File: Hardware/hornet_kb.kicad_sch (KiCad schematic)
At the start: 12 parts, among them J1 Conn_ST_STDC14, J10 USB_C_Receptacle_USB2.0, U1 nRF52840, Y1 32.768kHz, Y2 32MHz

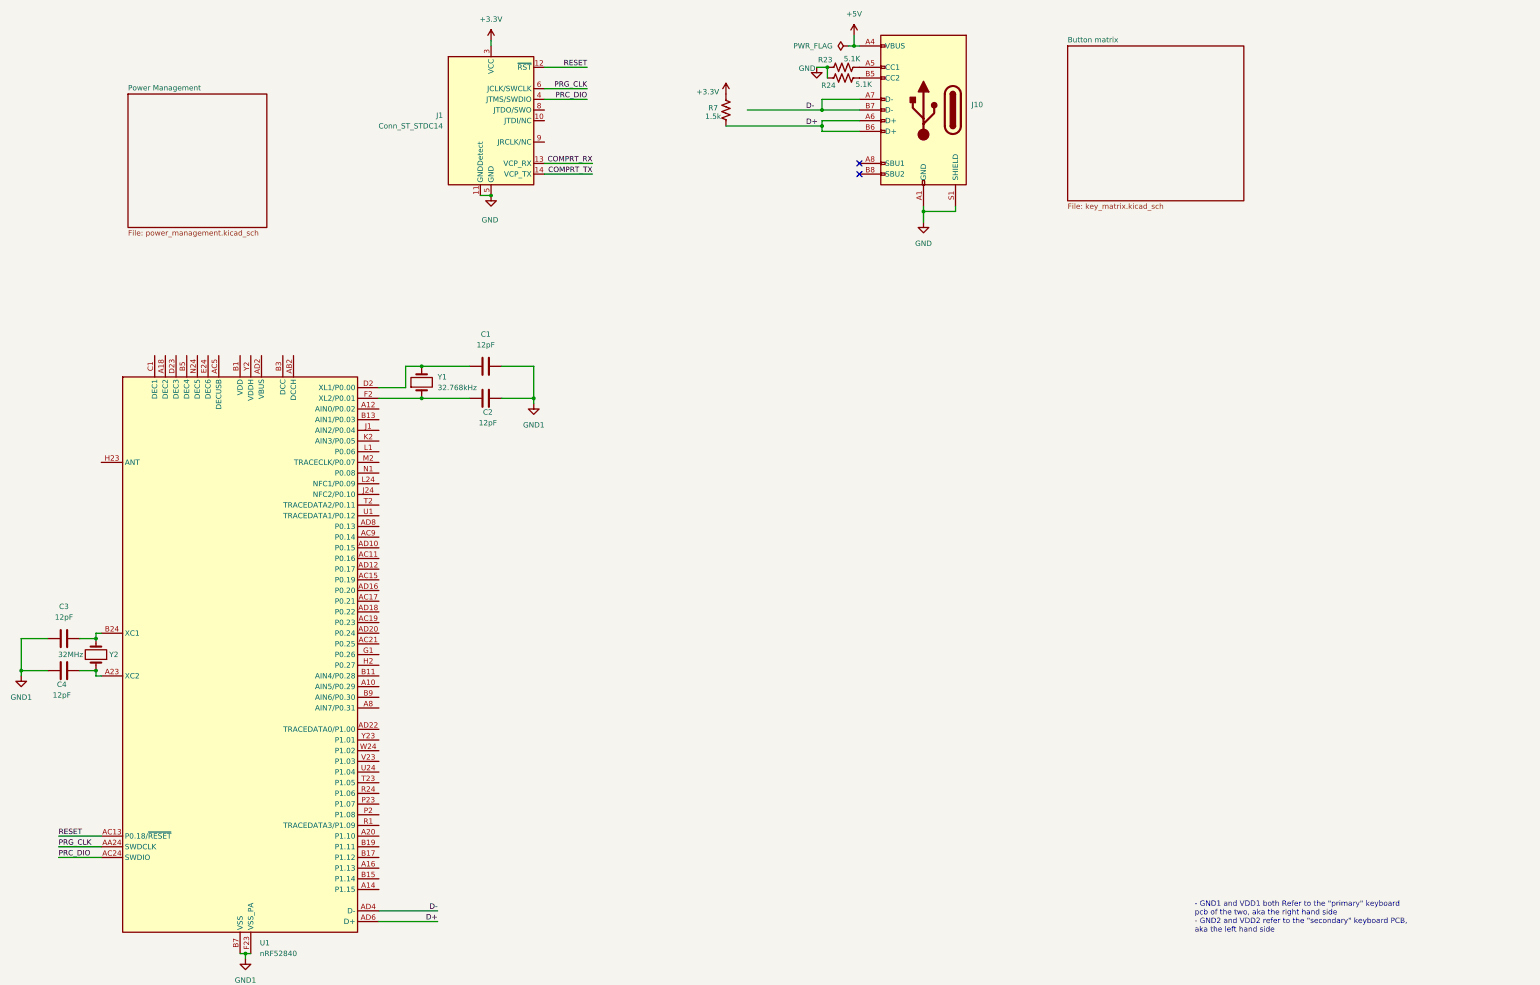
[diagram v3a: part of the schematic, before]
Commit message: Added external kicad library for niche ass footprints
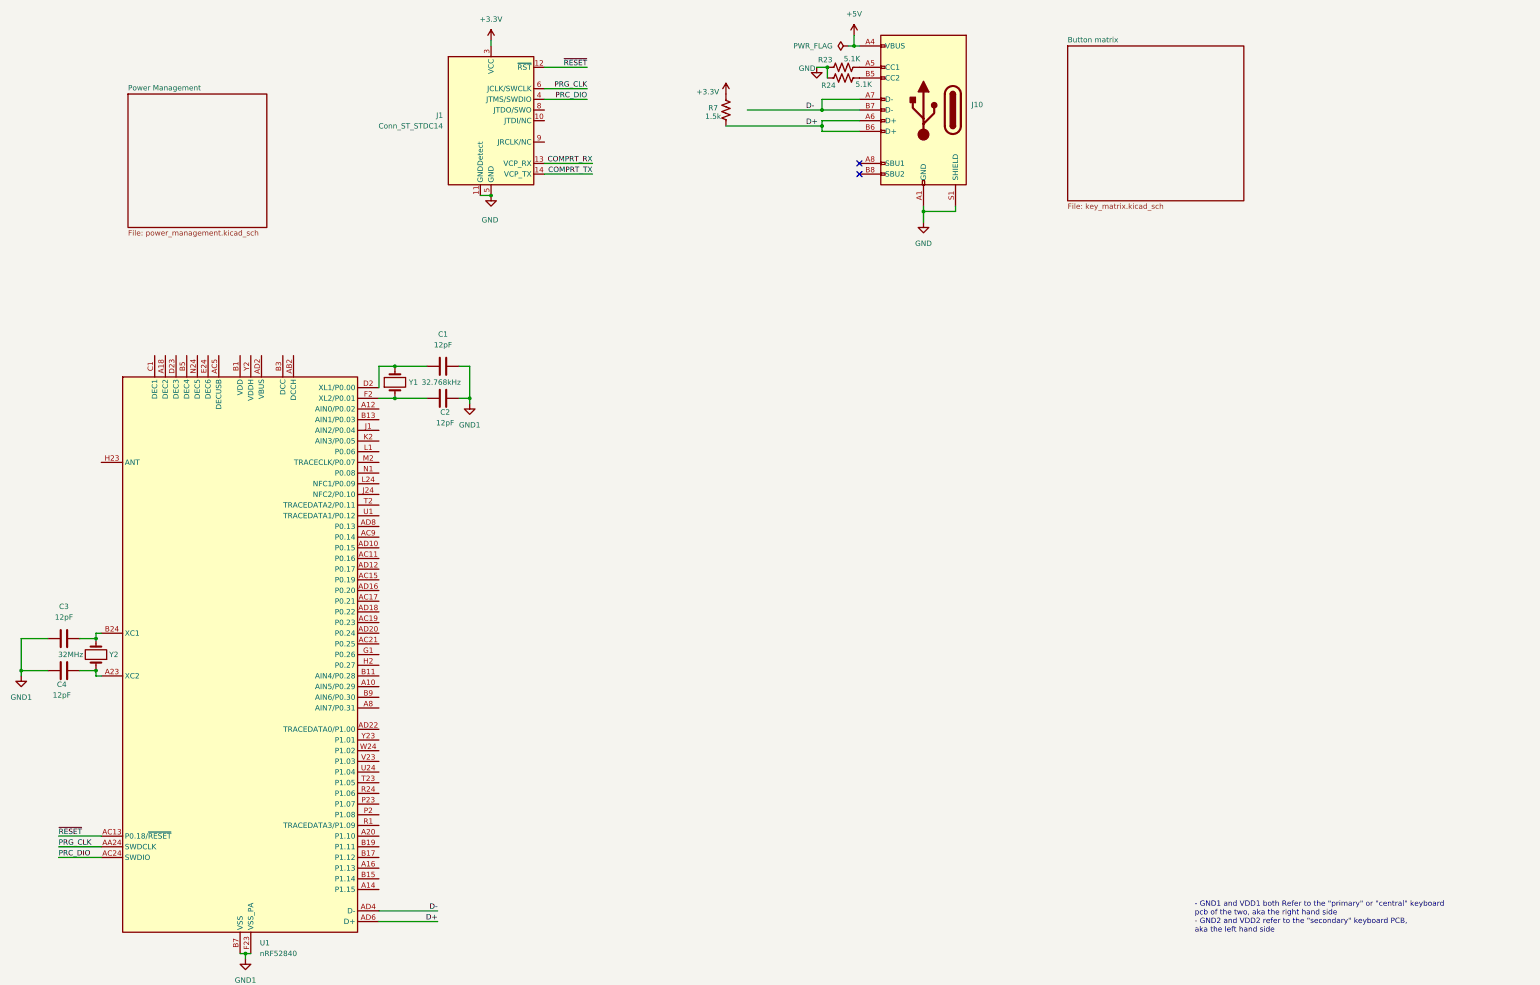
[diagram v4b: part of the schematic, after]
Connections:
- net RESET renamed ~{RESET}
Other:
- note added: "- GND1 and VDD1 both Refer to the "primary" or "central" keyboard pcb of the two, aka the right hand side - GND2 and VDD2 refer to the "secondary" keyboard PCB, aka the left hand side"
- note removed: "- GND1 and VDD1 both Refer to the "primary" keyboard pcb of the two, aka the right hand side - GND2 and VDD2 refer to the "secondary" keyboard PCB, aka the left hand side"
- moved on the sheet: C1, C2, Y1
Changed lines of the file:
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@@
 		(rev "Rev1")
 	)
-	(text "- GND1 and VDD1 both Refer to the \"primary\" keyboard \npcb of the two, aka the right hand side\n- GND2 and VDD2 refer to the \"secondary\" keyboard PCB,\naka the left hand side"
+	(text "- GND1 and VDD1 both Refer to the \"primary\" or \"central\" keyboard \npcb of the two, aka the right hand side\n- GND2 and VDD2 refer to the \"secondary\" keyboard PCB,\naka the left hand side"
 		(exclude_from_sim no)
 		(at 300.736 258.064 0)
@@
 	)
 	(junction
-		(at 116.84 134.62)
+		(at 110.49 134.62)
 		(diameter 0)
 		(color 0 0 0 0)
@@
 	)
 	(junction
-		(at 116.84 127)
+		(at 212.09 66.04)
 		(diameter 0)
 		(color 0 0 0 0)
 	)
 	(junction
-		(at 212.09 66.04)
+		(at 213.36 55.88)
 		(diameter 0)
 		(color 0 0 0 0)
 	)
 	(junction
-		(at 213.36 55.88)
+		(at 236.22 90.17)
 		(diameter 0)
 		(color 0 0 0 0)
 	)
 	(junction
-		(at 236.22 90.17)
+		(at 110.49 127)
 		(diameter 0)
 		(color 0 0 0 0)
 	)
 	(junction
-		(at 143.51 134.62)
+		(at 128.27 134.62)
 		(diameter 0)
 		(color 0 0 0 0)
@@
 	(wire
 		(pts
-			(xy 39.37 199.39) (xy 35.56 199.39)
+			(xy 106.68 127) (xy 106.68 132.08)
+		)
+		(stroke
+			(width 0)
+			(type default)
+		)
+	)
+	(wire
+		(pts
+			(xy 110.49 134.62) (xy 118.11 134.62)
 		)
 		(stroke
@@
 	(wire
 		(pts
-			(xy 106.68 134.62) (xy 116.84 134.62)
+			(xy 39.37 199.39) (xy 35.56 199.39)
 		)
 		(stroke
@@
 	(wire
 		(pts
-			(xy 143.51 134.62) (xy 135.89 134.62)
+			(xy 106.68 134.62) (xy 110.49 134.62)
 		)
 		(stroke
@@
 	(wire
 		(pts
-			(xy 143.51 134.62) (xy 143.51 135.89)
+			(xy 128.27 134.62) (xy 128.27 135.89)
 		)
 		(stroke
@@
 	(wire
 		(pts
-			(xy 30.48 243.84) (xy 40.64 243.84)
+			(xy 110.49 127) (xy 118.11 127)
 		)
 		(stroke
@@
 	(wire
 		(pts
-			(xy 219.71 50.8) (xy 220.98 50.8)
+			(xy 30.48 243.84) (xy 40.64 243.84)
 		)
 		(stroke
@@
 	(wire
 		(pts
-			(xy 157.48 78.74) (xy 146.05 78.74)
+			(xy 219.71 50.8) (xy 220.98 50.8)
 		)
 		(stroke
@@
 	(wire
 		(pts
-			(xy 113.03 127) (xy 113.03 132.08)
+			(xy 157.48 78.74) (xy 146.05 78.74)
 		)
 		(stroke
@@
 	(wire
 		(pts
-			(xy 113.03 132.08) (xy 106.68 132.08)
-		)
-		(stroke
-			(width 0)
-			(type default)
-		)
-	)
-	(wire
-		(pts
-			(xy 116.84 134.62) (xy 128.27 134.62)
+			(xy 106.68 127) (xy 110.49 127)
 		)
 		(stroke
@@
 	(wire
 		(pts
-			(xy 116.84 127) (xy 128.27 127)
-		)
-		(stroke
-			(width 0)
-			(type default)
-		)
-	)
-	(wire
-		(pts
 			(xy 21.59 199.39) (xy 27.94 199.39)
 		)
@@
 	(wire
 		(pts
-			(xy 143.51 127) (xy 143.51 134.62)
+			(xy 128.27 127) (xy 128.27 134.62)
 		)
 		(stroke
@@
 	(wire
 		(pts
-			(xy 243.84 90.17) (xy 236.22 90.17)
+			(xy 128.27 134.62) (xy 125.73 134.62)
 		)
 		(stroke
@@
 	(wire
 		(pts
-			(xy 143.51 127) (xy 135.89 127)
+			(xy 243.84 90.17) (xy 236.22 90.17)
 		)
 		(stroke
@@
 	(wire
 		(pts
-			(xy 113.03 127) (xy 116.84 127)
+			(xy 128.27 127) (xy 125.73 127)
 		)
 		(stroke
@@
 		)
 	)
-	(label "RESET"
-		(at 156.21 55.88 180)
+	(label "D+"
+		(at 208.28 69.85 0)
 		(effects
 			(font
 				(size 1.27 1.27)
 			)
-			(justify right bottom)
+			(justify left bottom)
 		)
 	)
-	(label "D+"
-		(at 208.28 69.85 0)
+	(label "COMPRT_TX"
+		(at 157.48 81.28 180)
 		(effects
 			(font
 				(size 1.27 1.27)
 			)
-			(justify left bottom)
+			(justify right bottom)
 		)
 	)
-	(label "COMPRT_TX"
-		(at 157.48 81.28 180)
+	(label "~{RESET}"
+		(at 156.21 55.88 180)
 		(effects
 			(font
@@
 		)
 	)
-	(label "RESET"
+	(label "~{RESET}"
 		(at 30.48 238.76 0)
 		(effects
@@
 	(symbol
 		(lib_id "Device:Crystal")
-		(at 116.84 130.81 90)
+		(at 110.49 130.81 90)
 		(unit 1)
 		(exclude_from_sim no)
@@
 		(on_board yes)
 		(dnp no)
-		(fields_autoplaced yes)
 		(property "Reference" "Y1"
-			(at 120.65 129.5399 90)
+			(at 113.792 130.81 90)
 			(effects
 				(font
@@
 		)
 		(property "Value" "32.768kHz"
-			(at 120.65 132.0799 90)
+			(at 116.84 130.81 90)
 			(effects
 				(font
@@
 		)
 		(property "Footprint" ""
-			(at 116.84 130.81 0)
+			(at 110.49 130.81 0)
 			(effects
 				(font
@@
 		)
 		(property "Datasheet" "~"
-			(at 116.84 130.81 0)
+			(at 110.49 130.81 0)
 			(effects
 				(font
@@
 		)
 		(property "Description" "Two pin crystal"
-			(at 116.84 130.81 0)
+			(at 110.49 130.81 0)
 			(effects
 				(font
@@
 	(symbol
 		(lib_id "power:GND1")
-		(at 143.51 135.89 0)
+		(at 128.27 135.89 0)
 		(unit 1)
 		(exclude_from_sim no)
@@
 		(fields_autoplaced yes)
 		(property "Reference" "#PWR02"
-			(at 143.51 142.24 0)
+			(at 128.27 142.24 0)
 			(effects
 				(font
@@
 		)
 		(property "Value" "GND1"
-			(at 143.51 140.97 0)
+			(at 128.27 140.97 0)
 			(effects
 				(font
@@
 		)
 		(property "Footprint" ""
-			(at 143.51 135.89 0)
+			(at 128.27 135.89 0)
 			(effects
 				(font
@@
 		)
 		(property "Datasheet" ""
-			(at 143.51 135.89 0)
+			(at 128.27 135.89 0)
 			(effects
 				(font
@@
 		)
 		(property "Description" "Power symbol creates a global label with name \"GND1\" , ground"
-			(at 143.51 135.89 0)
+			(at 128.27 135.89 0)
 			(effects
 				(font
@@
 	(symbol
 		(lib_id "Device:C")
-		(at 132.08 127 270)
+		(at 121.92 127 270)
 		(unit 1)
 		(exclude_from_sim no)
@@
 		(fields_autoplaced yes)
 		(property "Reference" "C1"
-			(at 132.08 119.38 90)
+			(at 121.92 119.38 90)
 			(effects
 				(font
@@
 		)
 		(property "Value" "12pF"
-			(at 132.08 121.92 90)
+			(at 121.92 121.92 90)
 			(effects
 				(font
@@
 		)
 		(property "Footprint" ""
-			(at 128.27 127.9652 0)
+			(at 118.11 127.9652 0)
 			(effects
 				(font
@@
 		)
 		(property "Datasheet" "~"
-			(at 132.08 127 0)
+			(at 121.92 127 0)
 			(effects
 				(font
@@
 		)
 		(property "Description" "Unpolarized capacitor"
-			(at 132.08 127 0)
+			(at 121.92 127 0)
 			(effects
 				(font
@@
 	(symbol
 		(lib_id "Device:C")
-		(at 132.08 134.62 270)
+		(at 121.92 134.62 270)
 		(unit 1)
 		(exclude_from_sim no)
@@
 		(dnp no)
 		(property "Reference" "C2"
-			(at 132.588 137.922 90)
+			(at 122.428 137.922 90)
 			(effects
 				(font
@@
 		)
 		(property "Value" "12pF"
-			(at 132.588 140.462 90)
+			(at 122.428 140.462 90)
 			(effects
 				(font
@@
 		)
 		(property "Footprint" ""
-			(at 128.27 135.5852 0)
+			(at 118.11 135.5852 0)
 			(effects
 				(font
@@
 		)
 		(property "Datasheet" "~"
-			(at 132.08 134.62 0)
+			(at 121.92 134.62 0)
 			(effects
 				(font
@@
 		)
 		(property "Description" "Unpolarized capacitor"
-			(at 132.08 134.62 0)
+			(at 121.92 134.62 0)
 			(effects
 				(font

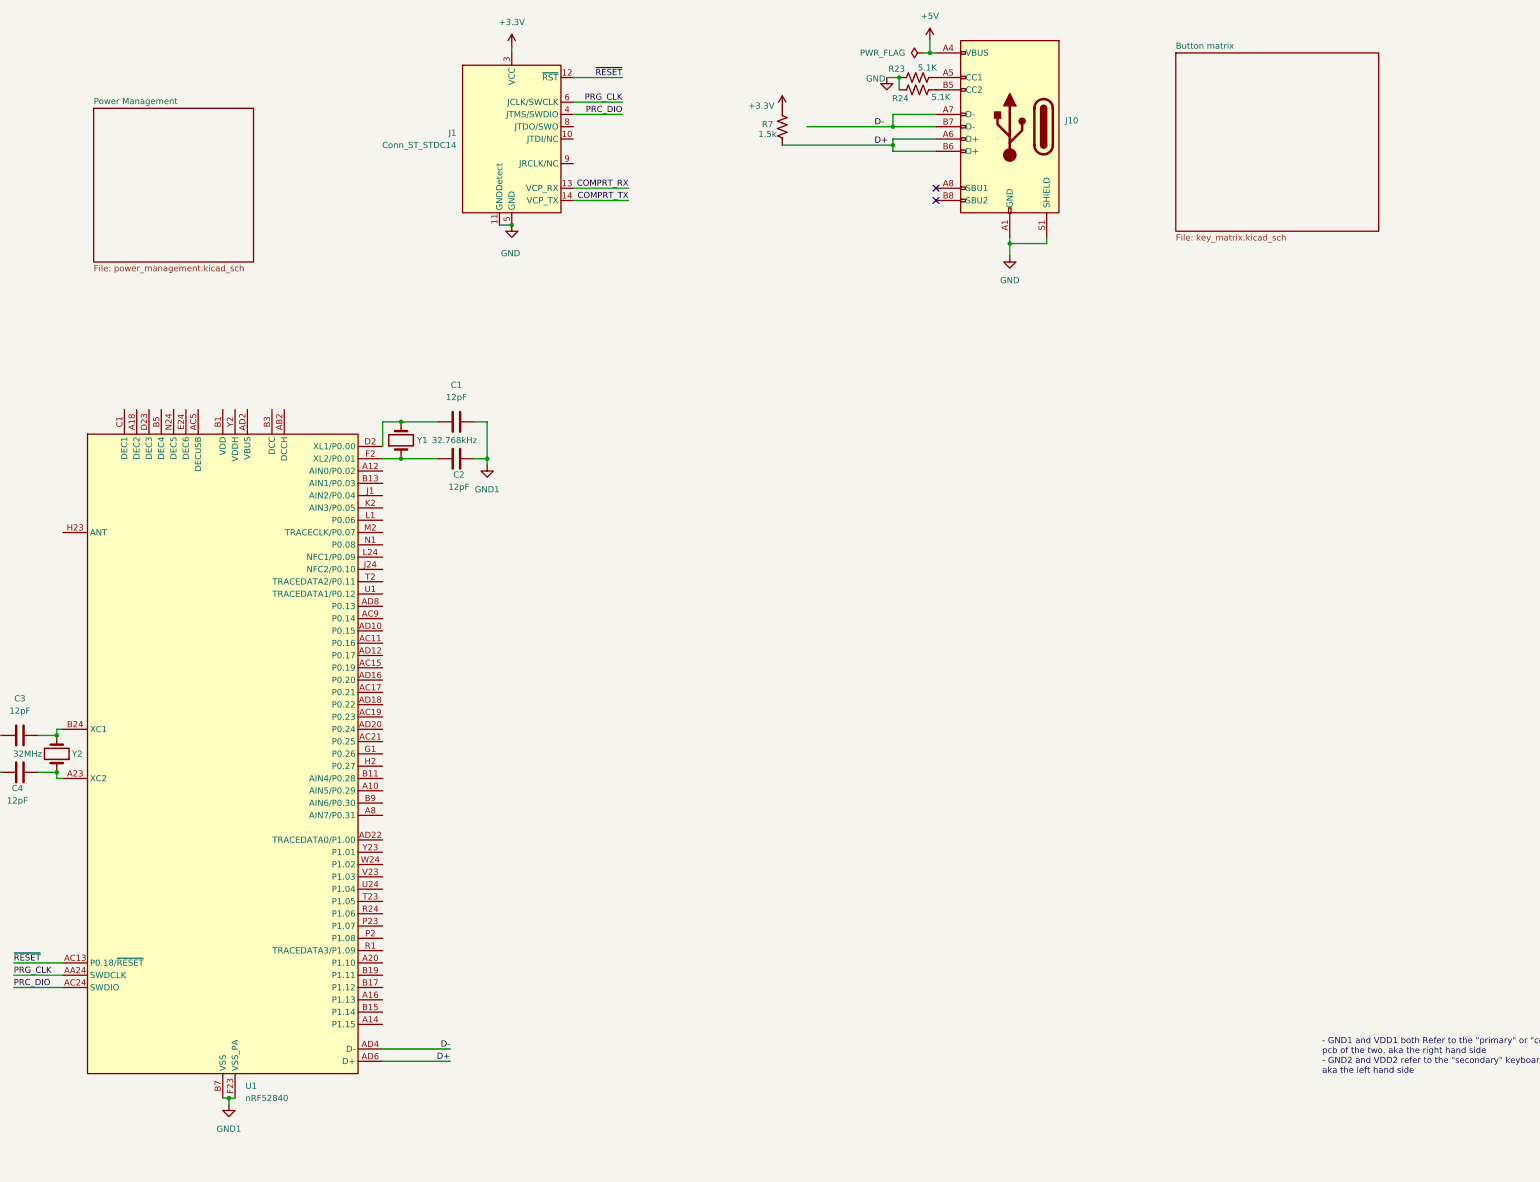
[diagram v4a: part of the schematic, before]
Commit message: Complete draft of key matrix for both sides
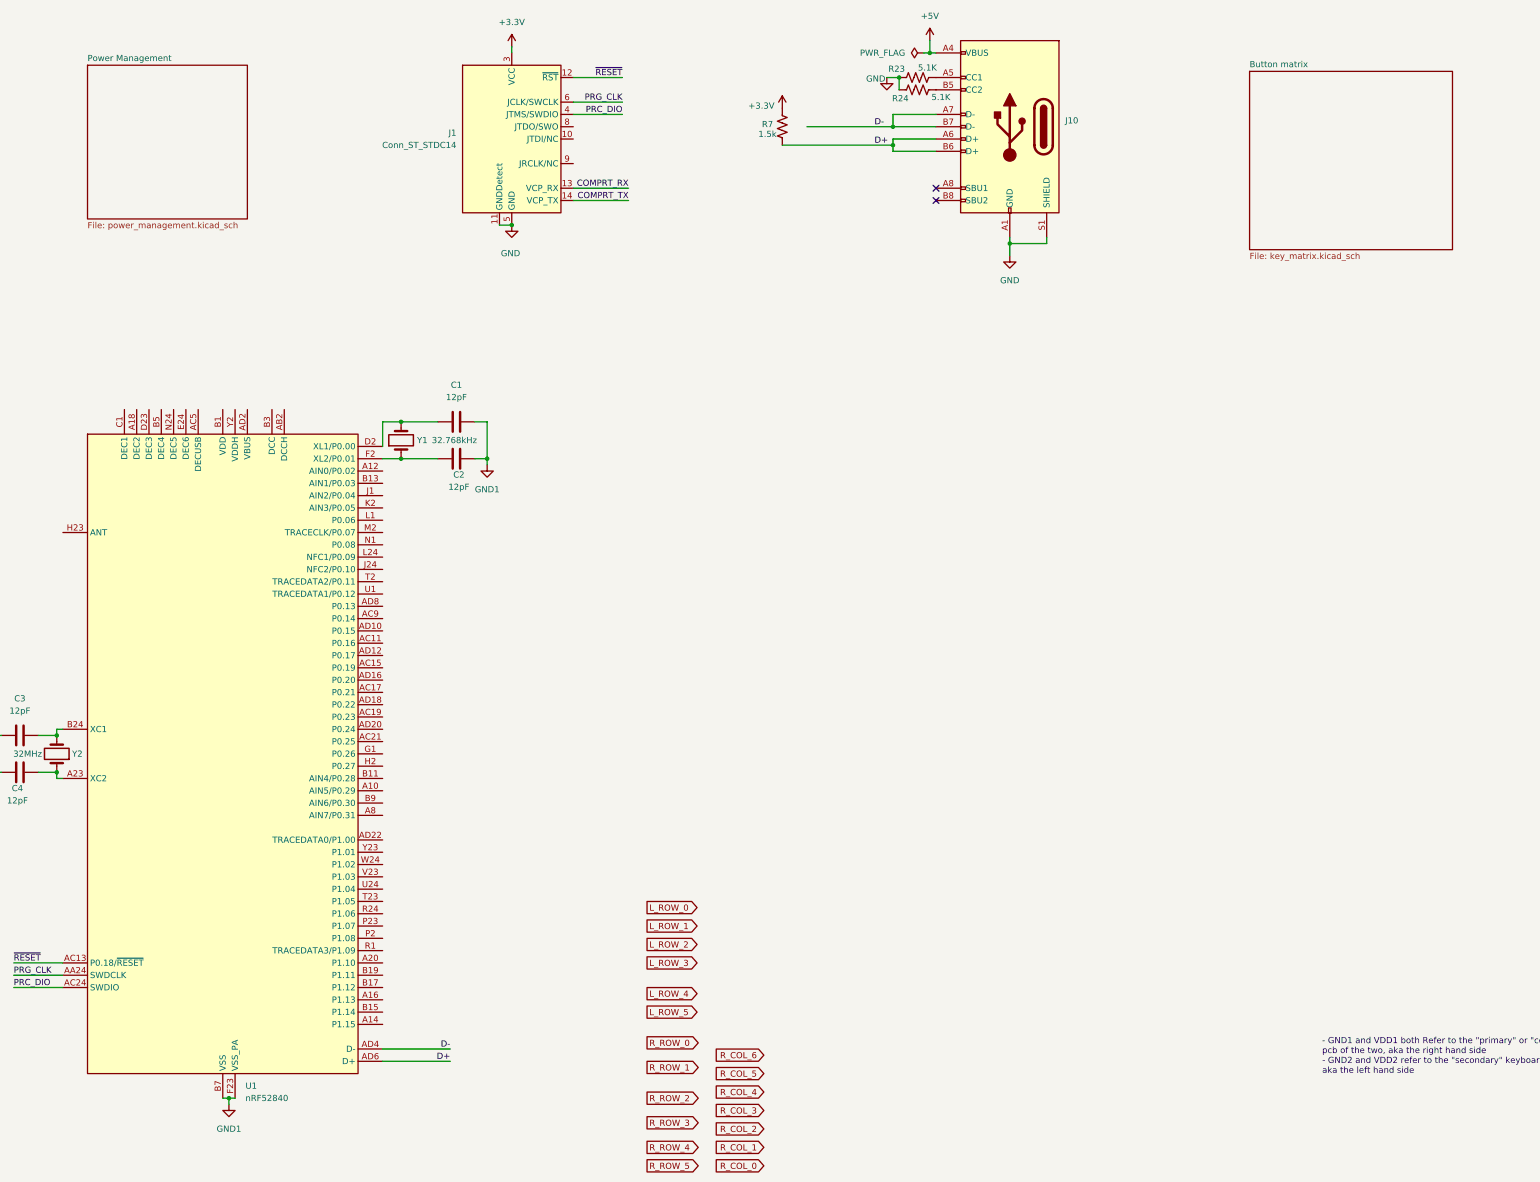
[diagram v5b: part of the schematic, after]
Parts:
- C1, C2, C3, C4: footprint (none) -> Capacitor_SMD:C_0402_1005Metric
- J1: footprint (none) -> Connector:Tag-Connect_TC2070-IDC-FP_2x07_P1.27mm_Vertical

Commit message: Added decoupling caps
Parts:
- added C10: 820pF, symbol Device:C
- added C12, C5: 4.7uF, symbol Device:C
- added C6: 100pF, symbol Device:C
- added C7: 100nF, symbol Device:C
- added C9: 0.1uF, symbol Device:C
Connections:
- net +5V is gone; now on net VBUS: J10.A4 (VBUS), J10.A9 (VBUS), J10.B4 (VBUS), J10.B9 (VBUS)
- net +3.3V: no longer J1.3 (VCC)
- net GND: no longer J1.11 (GNDDetect), J1.5 (GND), J1.7 (GND)
- net GND1: now also J1.11 (GNDDetect), J1.5 (GND), J1.7 (GND), C10.2, C12.2, C5.1, C6.2, C7.2, C9.2
- net R_COL_0: now also U1.H2 (P0.27)
- net R_COL_1: now also U1.G1 (P0.26)
- net R_COL_2: now also U1.AC21 (P0.25)
- net R_COL_3: now also U1.AD20 (P0.24)
- net R_COL_4: now also U1.AC19 (P0.23)
- net R_COL_5: now also U1.AD18 (P0.22)
- net R_COL_6: now also U1.AC17 (P0.21)
- net R_ROW_0: now also U1.AD8 (P0.13)
- net R_ROW_1: now also U1.AC9 (P0.14)
- net R_ROW_2: now also U1.AD10 (P0.15)
- net R_ROW_3: now also U1.AC11 (P0.16)
- net R_ROW_4: now also U1.AD12 (P0.17)
- net R_ROW_5: now also U1.AC15 (P0.19)
- net VDD: now reaches U1.A22 (VDD), U1.AD14 (VDD), U1.AD23 (VDD), U1.B1 (VDD), U1.W1 (VDD)
- net at U1.AC5 (DECUSB): now also C12.1
- net VBUS: now reaches U1.AD2 (VBUS)
- net VBUS: now also C5.2
- net at U1.B5 (DEC4): now also U1.E24 (DEC6), C9.1
- net at U1.C1 (DEC1): now also C7.1
- net at U1.D23 (DEC3): now also C6.1
- net at U1.N24 (DEC5): now also C10.1
- no-connect marks 2 -> 6
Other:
- note added: "decoupling caps routed as per pg 593"
- moved on the sheet: C1, C2, C3, C4, J1, J10, R23, R24, R7, U1, Y1, Y2
